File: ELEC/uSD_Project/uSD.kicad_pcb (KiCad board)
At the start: 2 copper layers, 50.8 x 39.4 mm, 5 parts, among them J1 CONN_01X08, U1 74HC595, U2 74HC165

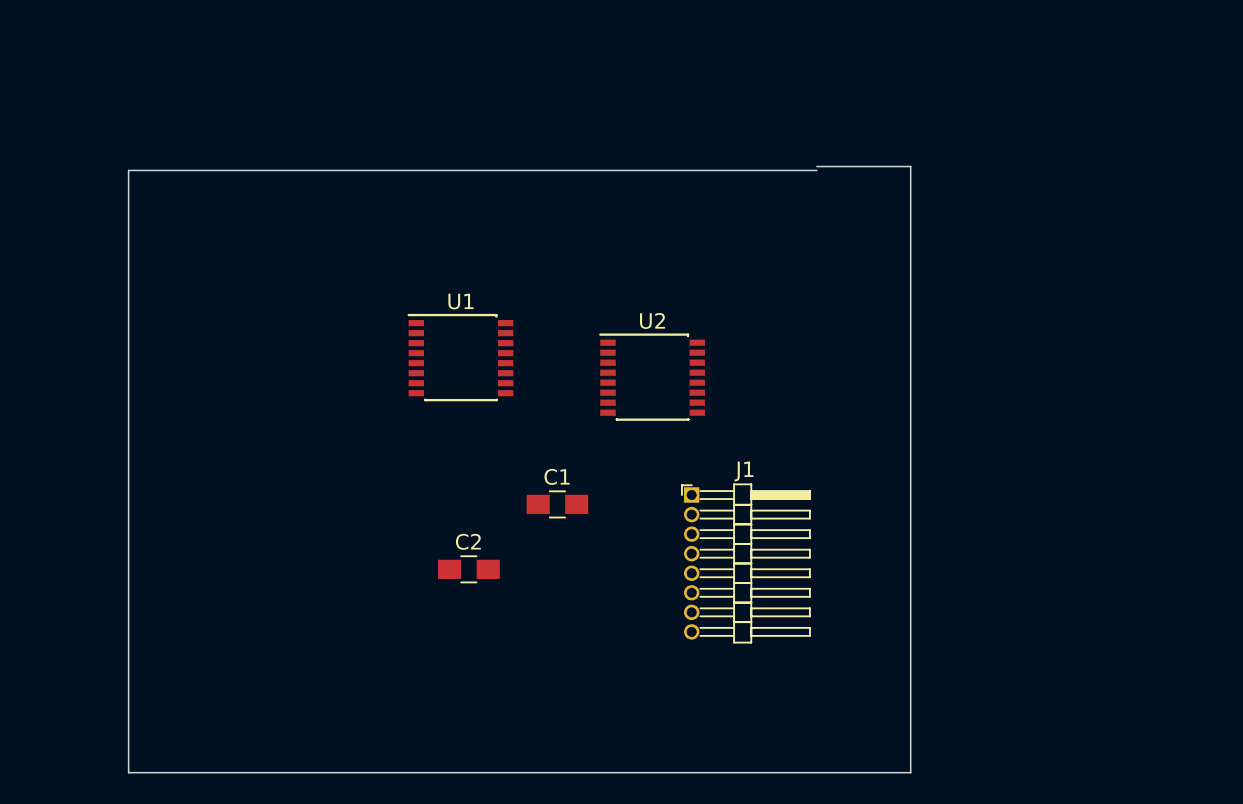
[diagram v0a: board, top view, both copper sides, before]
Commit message: Added uSD outline
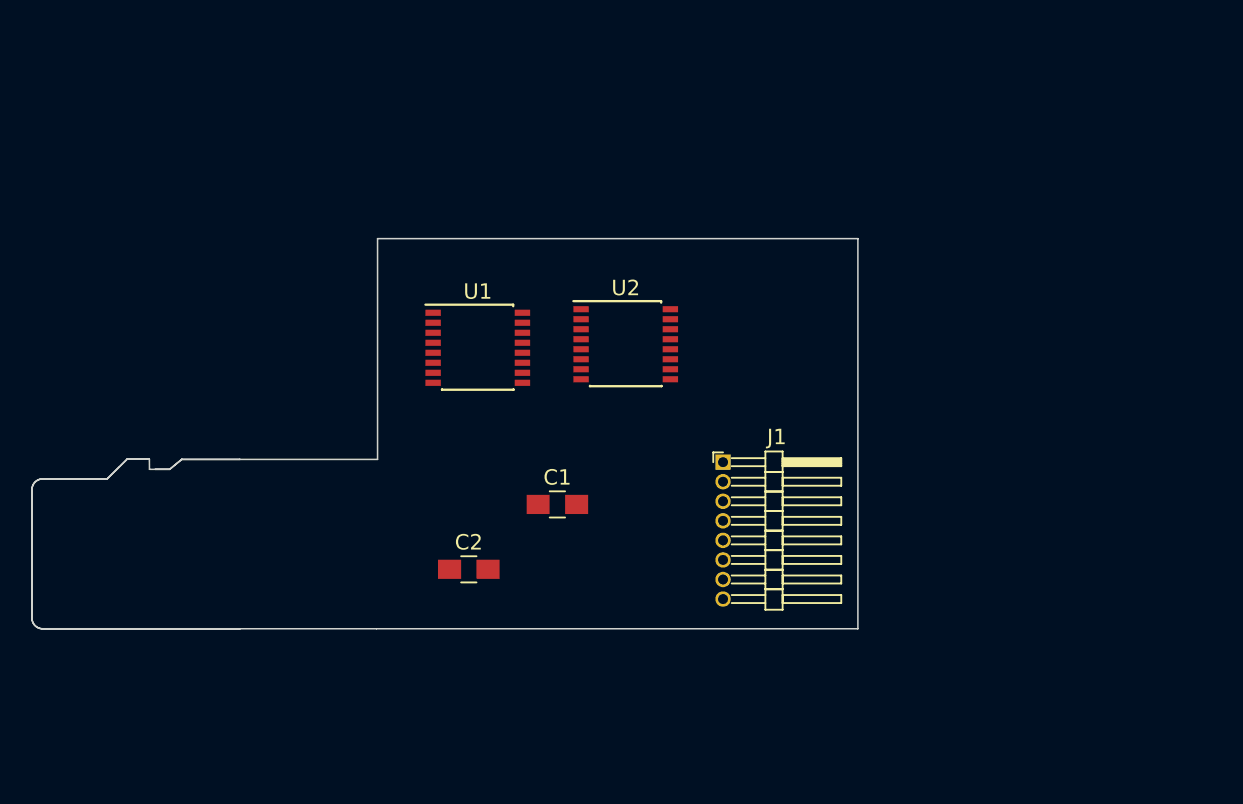
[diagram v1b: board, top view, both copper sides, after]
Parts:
- moved J1 2.95 mm to (159.3, 102.3)
- moved U2 2.79 mm to (152.9, 94.6)
- moved U1 1.28 mm to (143.3, 94.8)
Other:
- board size 50.8 x 39.4 mm -> 53.7 x 25.3 mm
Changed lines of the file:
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@@
     (links 5)
     (no_connects 5)
-    (area 138.364999 90.879 165.751834 115.994)
+    (area 114.317844 87.689999 168.070001 113.130001)
     (thickness 1.6)
-    (drawings 5)
+    (drawings 27)
     (tracks 0)
     (zones 0)
@@
   )
   (module Pin_Headers:Pin_Header_Angled_1x08_Pitch1.27mm (layer F.Cu)
-    (at 157.226 104.394)
+    (at 159.26 102.26)
     (descr "Through hole angled pin header, 1x08, 1.27mm pitch, 3.81mm pin length, single row")
     (tags "Through hole angled pin header THT 1x08 1.27mm single row")
@@
   )
   (module Housings_SSOP.pretty:SSOP-16_4.4x5.2mm_Pitch0.65mm (layer F.Cu)
-    (at 142.24 95.504)
+    (at 143.33 94.83)
     (descr "SSOP16: plastic shrink small outline package; 16 leads; body width 4.4 mm; (see NXP SSOP-TSSOP-VSO-REFLOW.pdf and sot369-1_po.pdf)")
     (tags "SSOP 0.65")
@@
   )
   (module Housings_SSOP.pretty:SSOP-16_4.4x5.2mm_Pitch0.65mm (layer F.Cu)
-    (at 154.686 96.774)
+    (at 152.94 94.6)
     (descr "SSOP16: plastic shrink small outline package; 16 leads; body width 4.4 mm; (see NXP SSOP-TSSOP-VSO-REFLOW.pdf and sot369-1_po.pdf)")
     (tags "SSOP 0.65")
@@
     )
   )
-  (gr_line (start 171.45 83.058) (end 165.354 83.058) (angle 90) (layer Edge.Cuts) (width 0.1))
-  (gr_line (start 171.45 122.428) (end 171.45 83.058) (angle 90) (layer Edge.Cuts) (width 0.1))
-  (gr_line (start 120.65 122.428) (end 171.45 122.428) (angle 90) (layer Edge.Cuts) (width 0.1))
-  (gr_line (start 120.65 83.312) (end 120.65 122.428) (angle 90) (layer Edge.Cuts) (width 0.1))
-  (gr_line (start 165.354 83.312) (end 120.65 83.312) (angle 90) (layer Edge.Cuts) (width 0.1))
+  (gr_line (start 168.02 113.08) (end 168.02 87.74) (angle 90) (layer Edge.Cuts) (width 0.1))
+  (gr_line (start 136.75 113.08) (end 168.02 113.08) (angle 90) (layer Edge.Cuts) (width 0.1))
+  (gr_line (start 127.89 113.08) (end 136.74 113.08) (angle 90) (layer Edge.Cuts) (width 0.1))
+  (gr_line (start 136.82 87.74) (end 168.02 87.74) (angle 90) (layer Edge.Cuts) (width 0.1))
+  (gr_line (start 136.82 102.08) (end 136.82 87.74) (angle 90) (layer Edge.Cuts) (width 0.1))
+  (gr_line (start 127.89 102.08) (end 136.82 102.08) (angle 90) (layer Edge.Cuts) (width 0.1))
+  (gr_arc (start 115.067845 112.379967) (end 114.367845 112.379967) (angle -90) (layer Edge.Cuts) (width 0.1))
+  (gr_arc (start 115.067845 104.048811) (end 115.067845 103.348811) (angle -90) (layer Edge.Cuts) (width 0.1))
+  (gr_line (start 114.367845 112.379967) (end 114.367845 104.048811) (layer Edge.Cuts) (width 0.1))
+  (gr_line (start 115.067845 113.079967) (end 127.883038 113.079967) (layer Edge.Cuts) (width 0.1))
+  (gr_line (start 119.257073 103.348811) (end 115.067845 103.348811) (layer Edge.Cuts) (width 0.1))
+  (gr_line (start 120.548559 102.067935) (end 119.257073 103.348811) (layer Edge.Cuts) (width 0.1))
+  (gr_line (start 121.999196 102.067935) (end 120.548559 102.067935) (layer Edge.Cuts) (width 0.1))
+  (gr_line (start 122.0046 102.724221) (end 121.999196 102.067935) (layer Edge.Cuts) (width 0.1))
+  (gr_line (start 123.31725 102.724221) (end 122.0046 102.724221) (layer Edge.Cuts) (width 0.1))
+  (gr_line (start 124.101146 102.07881) (end 123.31725 102.724221) (layer Edge.Cuts) (width 0.1))
+  (gr_line (start 124.101146 102.07881) (end 127.883038 102.07881) (layer Edge.Cuts) (width 0.1))
+  (gr_arc (start 115.07628 112.380843) (end 114.37112 112.380843) (angle -82.49841338) (layer Edge.Cuts) (width 0.1))
+  (gr_line (start 114.371125 104.050455) (end 114.37112 112.380843) (layer Edge.Cuts) (width 0.1))
+  (gr_arc (start 115.07628 104.047935) (end 114.984219 103.348811) (angle -82.70312595) (layer Edge.Cuts) (width 0.1))
+  (gr_line (start 119.257073 103.348811) (end 114.984219 103.348811) (layer Edge.Cuts) (width 0.1))
+  (gr_line (start 120.548559 102.067935) (end 119.257073 103.348811) (layer Edge.Cuts) (width 0.1))
+  (gr_line (start 121.999196 102.067935) (end 120.548559 102.067935) (layer Edge.Cuts) (width 0.1))
+  (gr_line (start 123.31725 102.724221) (end 122.373801 102.724221) (layer Edge.Cuts) (width 0.1))
+  (gr_line (start 124.101146 102.07881) (end 123.31725 102.724221) (layer Edge.Cuts) (width 0.1))
+  (gr_line (start 127.883038 102.07881) (end 124.101146 102.07881) (layer Edge.Cuts) (width 0.1))
+  (gr_line (start 114.984219 113.079967) (end 127.883038 113.079967) (layer Edge.Cuts) (width 0.1))
 )

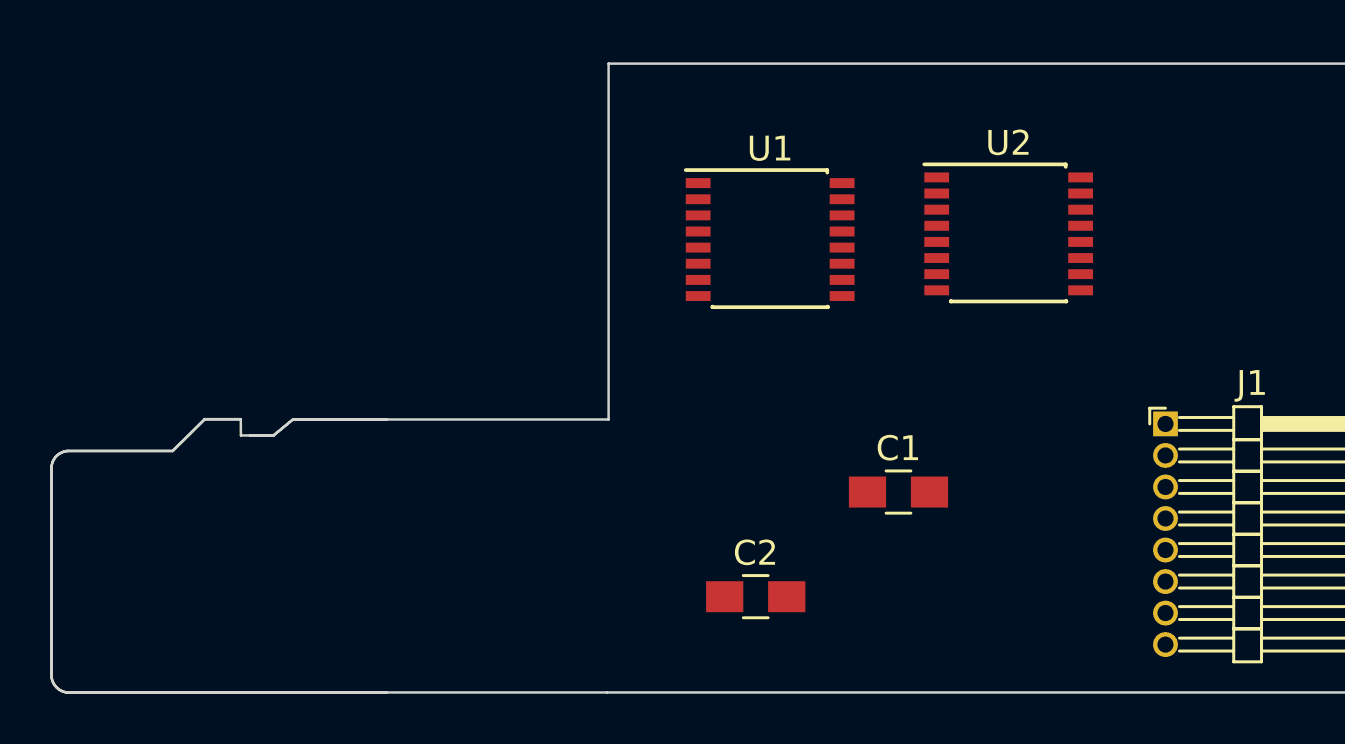
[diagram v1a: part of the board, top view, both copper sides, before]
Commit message: - Schematic capture - Creation of uSD part
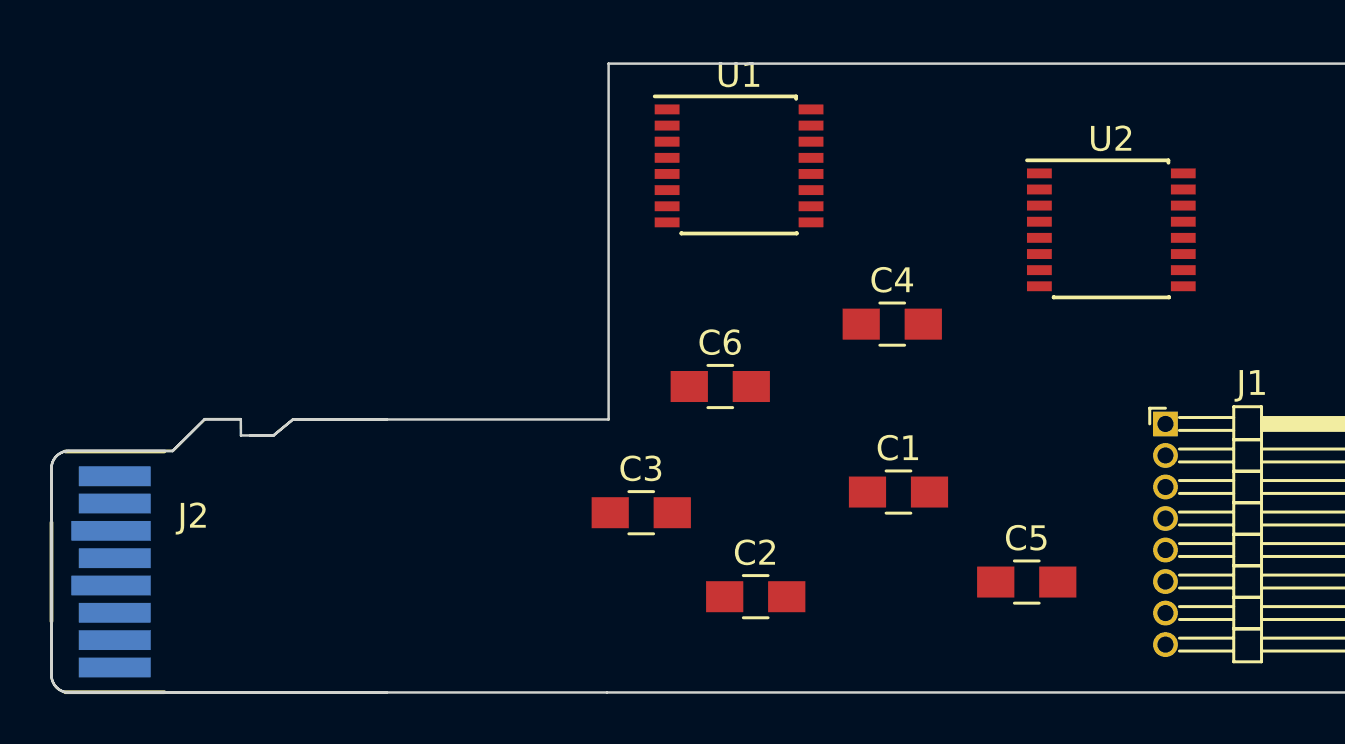
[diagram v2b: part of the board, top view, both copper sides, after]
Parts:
- added C3: 100nF, Capacitors_SMD:C_0805_HandSoldering, F.Cu at (138.1, 105.8)
- added C4: 1uF, Capacitors_SMD:C_0805_HandSoldering, F.Cu at (148.2, 98.2)
- added C5: 100nF, Capacitors_SMD:C_0805_HandSoldering, F.Cu at (153.7, 108.6)
- added C6: 1uF, Capacitors_SMD:C_0805_HandSoldering, F.Cu at (141.3, 100.8)
- added J2: CONN_01X08, Arranged_Pads.pretty:uSD, F.Cu at (116.9, 108.2)
- moved U2 4.14 mm to (157.1, 94.4)
- moved U1 3.22 mm to (142.1, 91.9)
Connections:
- net Net-(U1-Pad1) renamed /595_QB
- net Net-(U1-Pad11) renamed /SRCLK
- net Net-(U1-Pad14) renamed /Dat
- net Net-(U1-Pad15) renamed /595_QA
- net Net-(U1-Pad2) renamed /595_QC
- net Net-(U1-Pad3) renamed /595_QD
- net Net-(U1-Pad4) renamed /595_QE
- net Net-(U1-Pad5) renamed /595_QF
- net Net-(U1-Pad6) renamed /595_QG
- net Net-(U1-Pad7) renamed /595_QH
- net Net-(U2-Pad1) renamed /165_SHLD
- net Net-(U2-Pad11) renamed /165_A
- net Net-(U2-Pad12) renamed /165_B
- net Net-(U2-Pad13) renamed /165_C
- net Net-(U2-Pad14) renamed /165_D
- net Net-(U2-Pad2) renamed /165_CLK
- net Net-(U2-Pad3) renamed /165_E
- net Net-(U2-Pad4) renamed /165_F
- net Net-(U2-Pad5) renamed /165_G
- net Net-(U2-Pad6) renamed /165_H
- net Net-(U2-Pad9) renamed /165_Dat
- C1 pad 1: VDD -> VCC
- C2 pad 1: VDD -> VCC
- J1 pad 4: VDD -> VCC
- U1 pad 10: Net-(U1-Pad10) -> VCC
- U1 pad 12: Net-(U1-Pad12) -> //OE
- U1 pad 13: Net-(U1-Pad13) -> //OE
- U2 pad 15: Net-(U2-Pad15) -> GND
- U2 pad 16: Net-(U2-Pad16) -> VCC
- U2 pad 8: Net-(U2-Pad8) -> GND

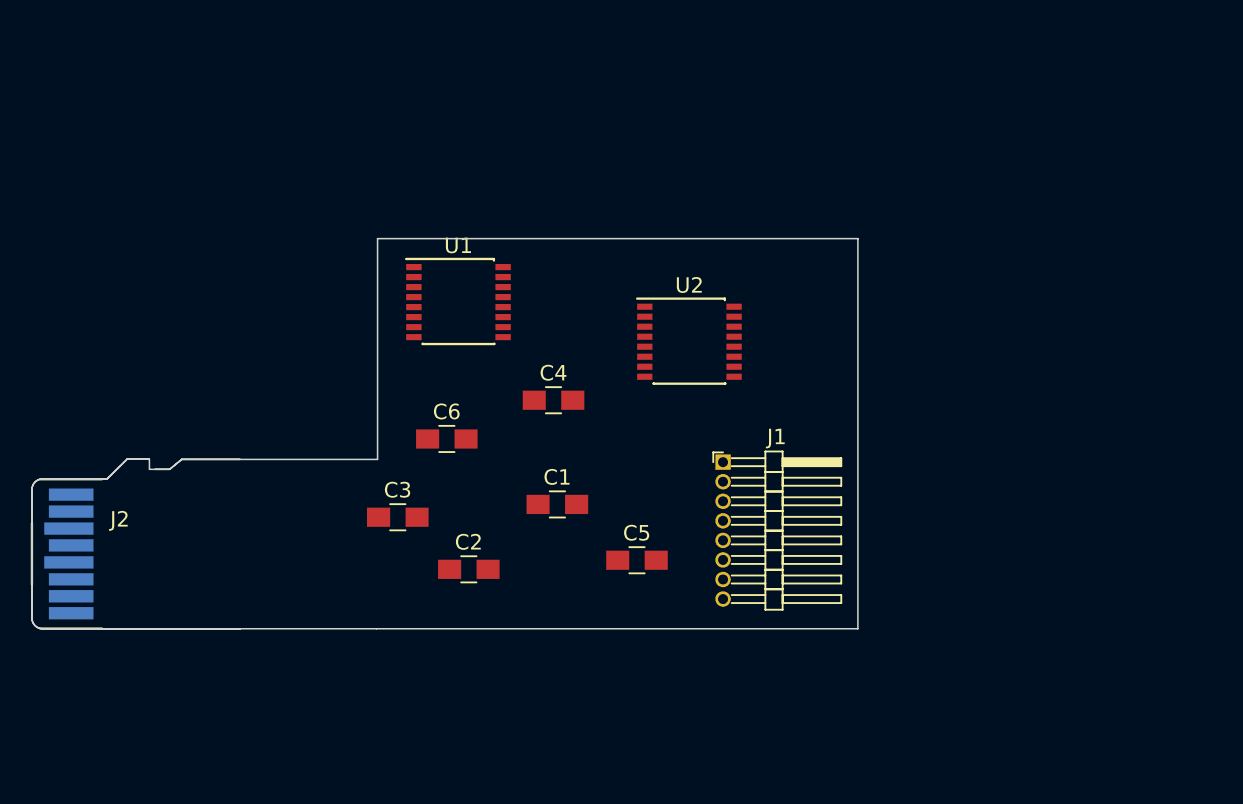
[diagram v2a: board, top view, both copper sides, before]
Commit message: Added padi stamp to project, moved some parts around, added pin headers, fixed net labels for shift reg etc...
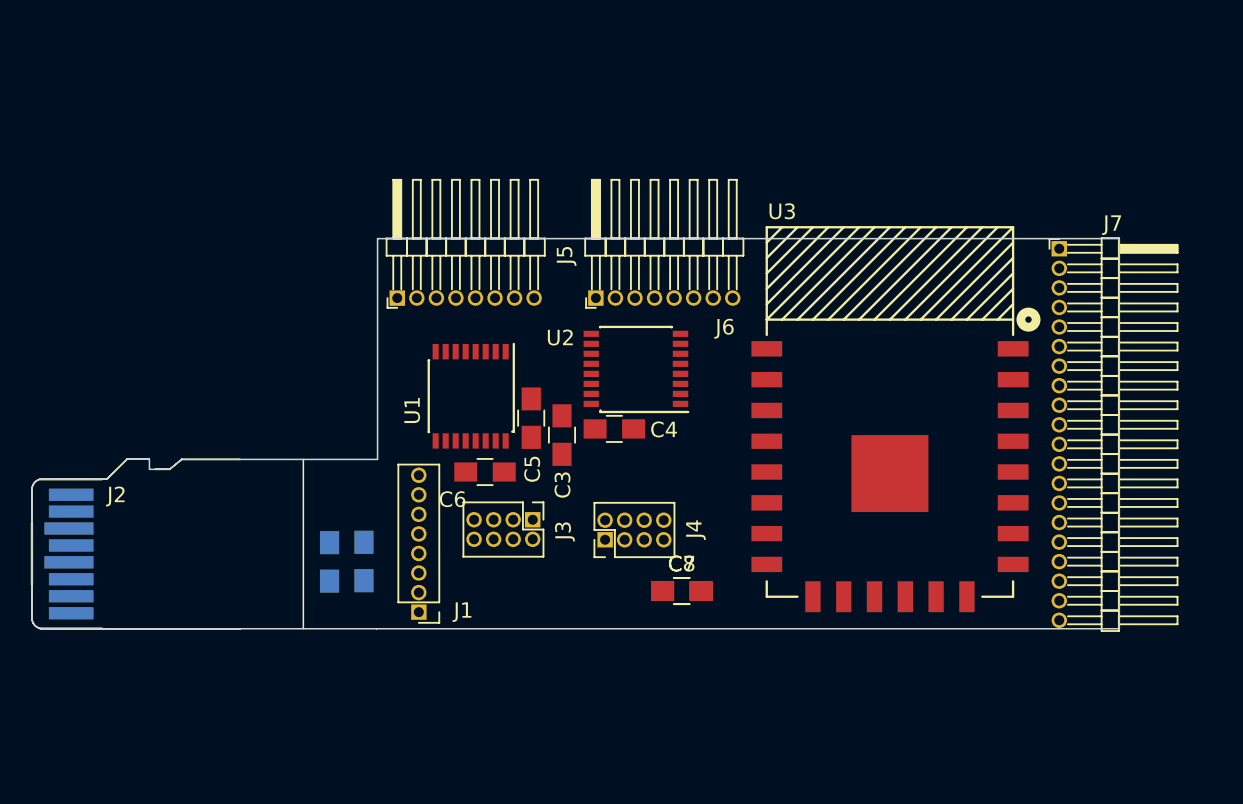
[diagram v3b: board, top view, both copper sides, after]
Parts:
- added C7: 100nF, Capacitors_SMD:C_0805_HandSoldering, F.Cu at (156.6, 110.6)
- added C8: 1uF, Capacitors_SMD:C_0805_HandSoldering, F.Cu at (156.6, 110.6)
- added J3: CONN_02X04, Pin_Headers:Pin_Header_Straight_2x04_Pitch1.27mm, F.Cu at (146.9, 106.0)
- added J4: CONN_02X04, Pin_Headers:Pin_Header_Straight_2x04_Pitch1.27mm, F.Cu at (151.6, 107.3)
- added J5: CONN_01X08, Pin_Headers:Pin_Header_Angled_1x08_Pitch1.27mm, F.Cu at (138.1, 91.6)
- added J6: CONN_01X08, Pin_Headers:Pin_Header_Angled_1x08_Pitch1.27mm, F.Cu at (151.0, 91.6)
- added J7: CONN_01X20, Pin_Headers:Pin_Header_Angled_1x20_Pitch1.27mm, F.Cu at (181.1, 88.4)
- added U3: PADI_IoT_Stamp, modules:PADI_IoT_Stamp, F.Cu at (162.1, 111.0)
- C1, C2: moved to B.Cu
- J1: footprint Pin_Headers:Pin_Header_Angled_1x08_Pitch1.27mm -> Pin_Headers:Pin_Header_Straight_1x08_Pitch1.27mm
- moved J1 22.0 mm to (139.5, 112.0), turned to 180 degrees
- moved C1 15.3 mm to (133.7, 108.7), turned to 270 degrees
- moved C3 11.9 mm to (148.8, 100.5), turned to 270 degrees
- moved C5 11.5 mm to (146.8, 99.4), turned to 90 degrees
- moved C2 6.83 mm to (135.9, 108.7), turned to 270 degrees
- moved U1 6.17 mm to (142.9, 98.0), turned to 270 degrees
- moved C4 4.37 mm to (152.2, 100.1)
- moved U2 3.90 mm to (153.6, 96.2), turned to 180 degrees
- moved C6 3.28 mm to (143.8, 102.9)
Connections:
- net //OE renamed /595_/OE
- J2 pad 1: /NC -> /RSV
- J2 pad 2: //CS -> /DO
- J2 pad 3: /DI -> GND
- J2 pad 4: VCC -> /CLK
- J2 pad 5: /CLK -> VCC
- J2 pad 6: GND -> /DI
- J2 pad 7: /DO -> //CS
- J2 pad 8: /RSV -> /NC
- U1 pad 11: /SRCLK -> /595_SRCLK
- U1 pad 14: /Dat -> /595_Dat
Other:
- board size 53.7 x 25.3 mm -> 70.6 x 25.3 mm
